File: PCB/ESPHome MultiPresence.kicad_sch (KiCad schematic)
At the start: 0 parts

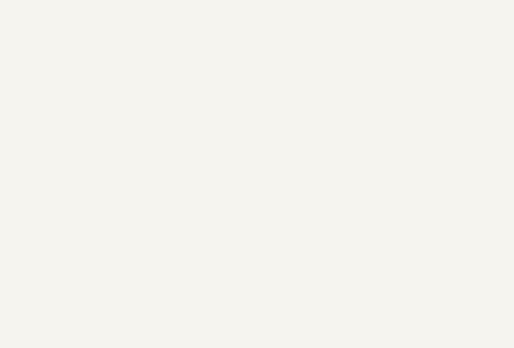
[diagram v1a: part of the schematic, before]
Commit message: updated footprints and started board layout
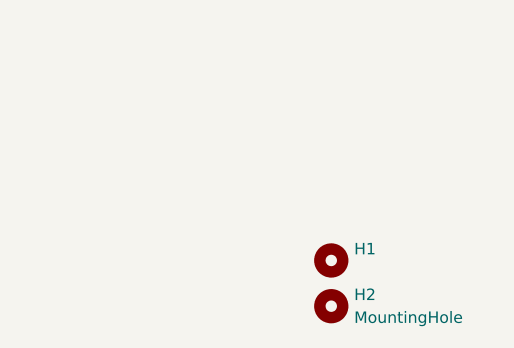
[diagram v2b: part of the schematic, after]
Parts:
- added H1: (no value), symbol Mechanical:MountingHole
- added H2: MountingHole, symbol Mechanical:MountingHole

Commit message: board layout work
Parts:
- H1: value (none) -> MountingHole; footprint (none) -> MountingHole:MountingHole_3.2mm_M3_Pad_Via
- H2: footprint (none) -> MountingHole:MountingHole_3.2mm_M3_Pad_Via
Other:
- moved on the sheet: H1, H2
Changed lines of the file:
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@@
     (effects (font (size 1.27 1.27)) (justify left bottom))
   )
-  (symbol (lib_id "Mechanical:MountingHole") (at 142.24 179.07 0) (unit 1)
+  (symbol (lib_id "Mechanical:MountingHole") (at 139.7 171.45 0) (unit 1)
     (in_bom yes) (on_board yes) (fields_autoplaced)
-    (property "Reference" "H2" (id 0) (at 144.78 177.7999 0)
-      (effects (font (size 1.27 1.27)) (justify left))
-    )
-    (property "Value" "MountingHole" (id 1) (at 144.78 180.3399 0)
-      (effects (font (size 1.27 1.27)) (justify left))
-    )
-    (property "Footprint" "" (id 2) (at 142.24 179.07 0)
-      (effects (font (size 1.27 1.27)) hide)
-    )
-    (property "Datasheet" "~" (id 3) (at 142.24 179.07 0)
-      (effects (font (size 1.27 1.27)) hide)
-    )
-  )
-  (symbol (lib_id "Mechanical:MountingHole") (at 142.24 173.99 0) (unit 1)
+    (property "Reference" "H2" (id 0) (at 142.24 170.1799 0)
+      (effects (font (size 1.27 1.27)) (justify left))
+    )
+    (property "Value" "MountingHole" (id 1) (at 142.24 172.7199 0)
+      (effects (font (size 1.27 1.27)) (justify left))
+    )
+    (property "Footprint" "MountingHole:MountingHole_3.2mm_M3_Pad_Via" (id 2) (at 139.7 171.45 0)
+      (effects (font (size 1.27 1.27)) hide)
+    )
+    (property "Datasheet" "~" (id 3) (at 139.7 171.45 0)
+      (effects (font (size 1.27 1.27)) hide)
+    )
+  )
+  (symbol (lib_id "Mechanical:MountingHole") (at 139.7 166.37 0) (unit 1)
     (in_bom yes) (on_board yes) (fields_autoplaced)
-    (property "Reference" "H1" (id 0) (at 144.78 172.7199 0)
-      (effects (font (size 1.27 1.27)) (justify left))
-    )
-    (property "Value" "" (id 1) (at 144.78 175.2599 0)
-      (effects (font (size 1.27 1.27)) (justify left))
-    )
-    (property "Footprint" "" (id 2) (at 142.24 173.99 0)
-      (effects (font (size 1.27 1.27)) hide)
-    )
-    (property "Datasheet" "~" (id 3) (at 142.24 173.99 0)
+    (property "Reference" "H1" (id 0) (at 142.24 165.0999 0)
+      (effects (font (size 1.27 1.27)) (justify left))
+    )
+    (property "Value" "MountingHole" (id 1) (at 142.24 167.6399 0)
+      (effects (font (size 1.27 1.27)) (justify left))
+    )
+    (property "Footprint" "MountingHole:MountingHole_3.2mm_M3_Pad_Via" (id 2) (at 139.7 166.37 0)
+      (effects (font (size 1.27 1.27)) hide)
+    )
+    (property "Datasheet" "~" (id 3) (at 139.7 166.37 0)
       (effects (font (size 1.27 1.27)) hide)
     )
@@
       (reference "TP4") (unit 1) (value "TestPoint") (footprint "TestPoint:TestPoint_THTPad_2.0x2.0mm_Drill1.0mm")
     )
-    (path "/02e06518-bdda-448b-8333-c04796006756/dea33614-e878-4b0e-b32f-24283ea1df53"
+    (path "/fb6bc2b2-fb70-4cbc-8144-2f6085fecaff/76fbd85d-2265-4697-9aca-f5babf51bf6b"
       (reference "TP5") (unit 1) (value "TestPoint") (footprint "TestPoint:TestPoint_THTPad_2.0x2.0mm_Drill1.0mm")
     )
-    (path "/02e06518-bdda-448b-8333-c04796006756/cede1638-147d-4c1d-b756-c02b8befeb06"
+    (path "/fb6bc2b2-fb70-4cbc-8144-2f6085fecaff/2ad961ac-0e85-4b4f-8f71-a006845292ba"
       (reference "TP6") (unit 1) (value "TestPoint") (footprint "TestPoint:TestPoint_THTPad_2.0x2.0mm_Drill1.0mm")
     )
-    (path "/fb6bc2b2-fb70-4cbc-8144-2f6085fecaff/76fbd85d-2265-4697-9aca-f5babf51bf6b"
+    (path "/fb6bc2b2-fb70-4cbc-8144-2f6085fecaff/670102d9-cbe5-41bf-8851-41b4b366cc52"
       (reference "TP7") (unit 1) (value "TestPoint") (footprint "TestPoint:TestPoint_THTPad_2.0x2.0mm_Drill1.0mm")
     )
-    (path "/fb6bc2b2-fb70-4cbc-8144-2f6085fecaff/2ad961ac-0e85-4b4f-8f71-a006845292ba"
+    (path "/fb6bc2b2-fb70-4cbc-8144-2f6085fecaff/233ffb6e-eb9f-4953-8272-983c6e32e87c"
       (reference "TP8") (unit 1) (value "TestPoint") (footprint "TestPoint:TestPoint_THTPad_2.0x2.0mm_Drill1.0mm")
     )
-    (path "/fb6bc2b2-fb70-4cbc-8144-2f6085fecaff/670102d9-cbe5-41bf-8851-41b4b366cc52"
+    (path "/fb6bc2b2-fb70-4cbc-8144-2f6085fecaff/68d7f3ec-1207-4e95-99cb-36bf5ed22008"
       (reference "TP9") (unit 1) (value "TestPoint") (footprint "TestPoint:TestPoint_THTPad_2.0x2.0mm_Drill1.0mm")
-    )
-    (path "/fb6bc2b2-fb70-4cbc-8144-2f6085fecaff/233ffb6e-eb9f-4953-8272-983c6e32e87c"
-      (reference "TP10") (unit 1) (value "TestPoint") (footprint "TestPoint:TestPoint_THTPad_2.0x2.0mm_Drill1.0mm")
-    )
-    (path "/fb6bc2b2-fb70-4cbc-8144-2f6085fecaff/68d7f3ec-1207-4e95-99cb-36bf5ed22008"
-      (reference "TP11") (unit 1) (value "TestPoint") (footprint "TestPoint:TestPoint_THTPad_2.0x2.0mm_Drill1.0mm")
     )
     (path "/02e06518-bdda-448b-8333-c04796006756/11cd4b94-6488-4d48-bcae-e0cd312e4262"
@@
       (reference "U3") (unit 1) (value "SEN0395") (footprint "My Footprints:SEN0395")
     )
+    (path "/fb6bc2b2-fb70-4cbc-8144-2f6085fecaff/b7ec94eb-e377-4843-a9d4-6c4661f41afb"
+      (reference "U4") (unit 1) (value "SHTC3") (footprint "Sensor_Humidity:Sensirion_DFN-4-1EP_2x2mm_P1mm_EP0.7x1.6mm")
+    )
     (path "/fb6bc2b2-fb70-4cbc-8144-2f6085fecaff/911f9e01-2092-4b84-875e-780e655575ff"
-      (reference "U4") (unit 1) (value "SEN0395") (footprint "My Footprints:SEN0395")
-    )
-    (path "/fb6bc2b2-fb70-4cbc-8144-2f6085fecaff/b7ec94eb-e377-4843-a9d4-6c4661f41afb"
-      (reference "U5") (unit 1) (value "SHTC3") (footprint "Sensor_Humidity:Sensirion_DFN-4-1EP_2x2mm_P1mm_EP0.7x1.6mm")
+      (reference "U5") (unit 1) (value "SEN0395") (footprint "My Footprints:SEN0395")
     )
     (path "/fb6bc2b2-fb70-4cbc-8144-2f6085fecaff/6393d8e9-e648-458f-87c0-4dab83b80f3c"
